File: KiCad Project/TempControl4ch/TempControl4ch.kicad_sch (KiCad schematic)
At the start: 44 parts, among them J1 Conn_01x08_Socket, U1 MAX31856, U2 MAX31856, U3 MAX31856, U4 MAX31856, U5 BluePill_Part_Like_SWD_Breako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

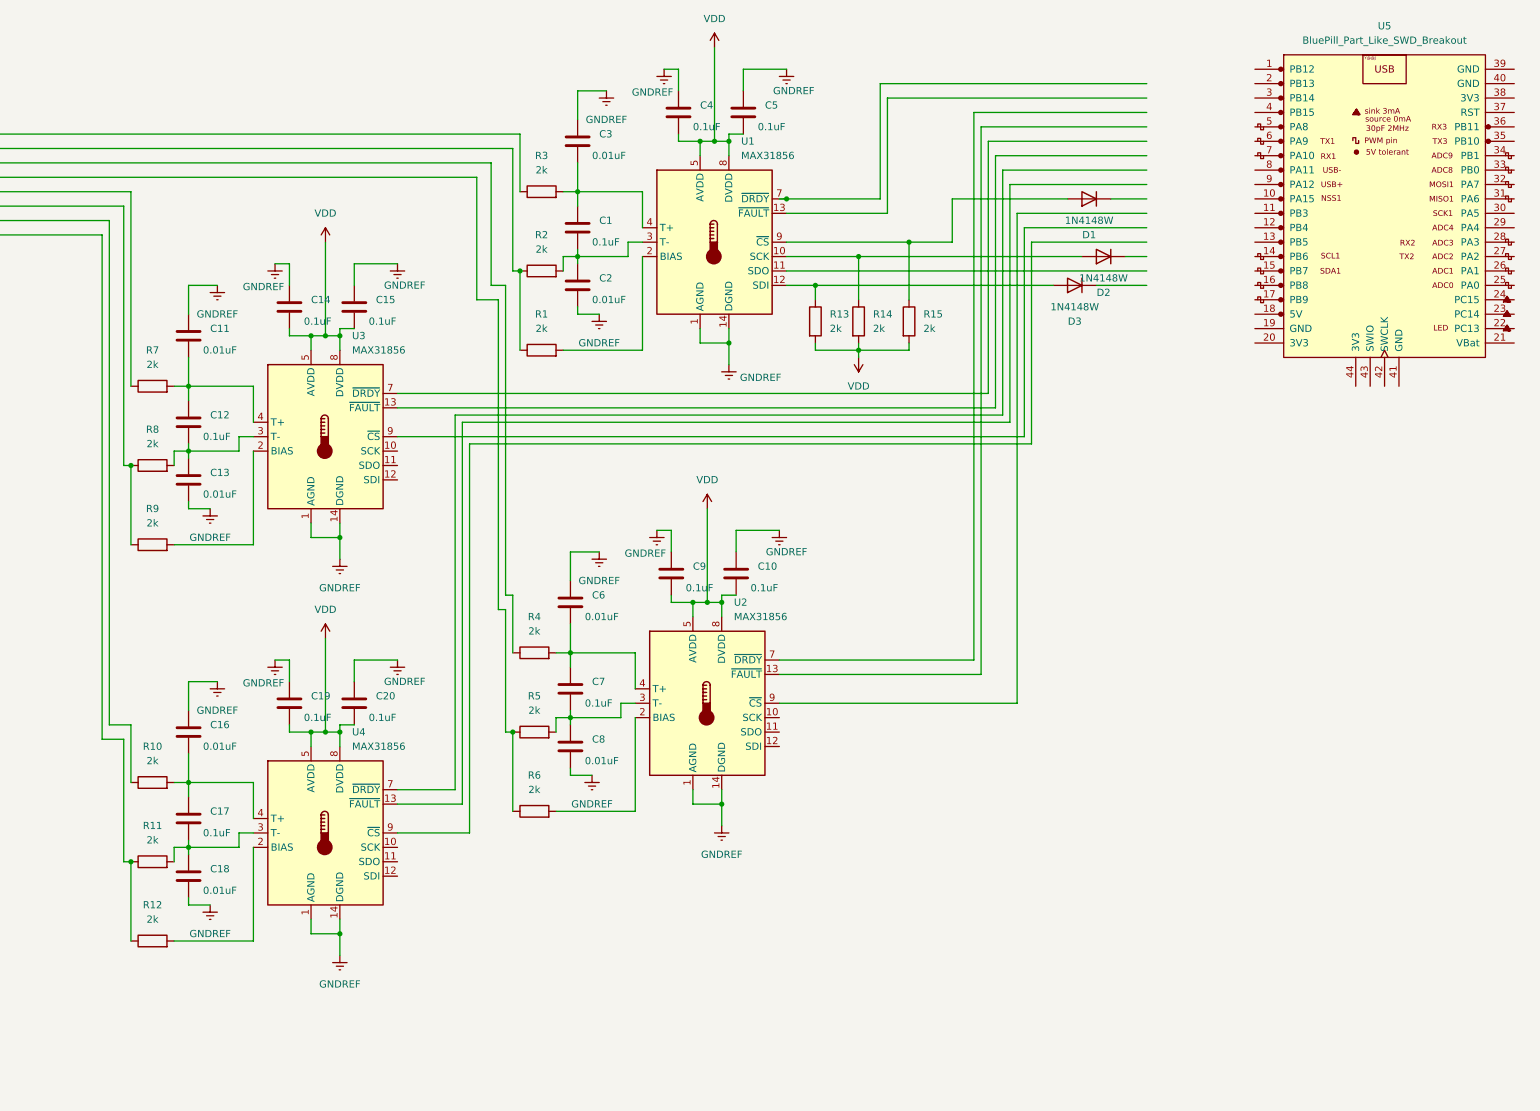
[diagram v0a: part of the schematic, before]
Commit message: added SPI connections and update schematic & pcb
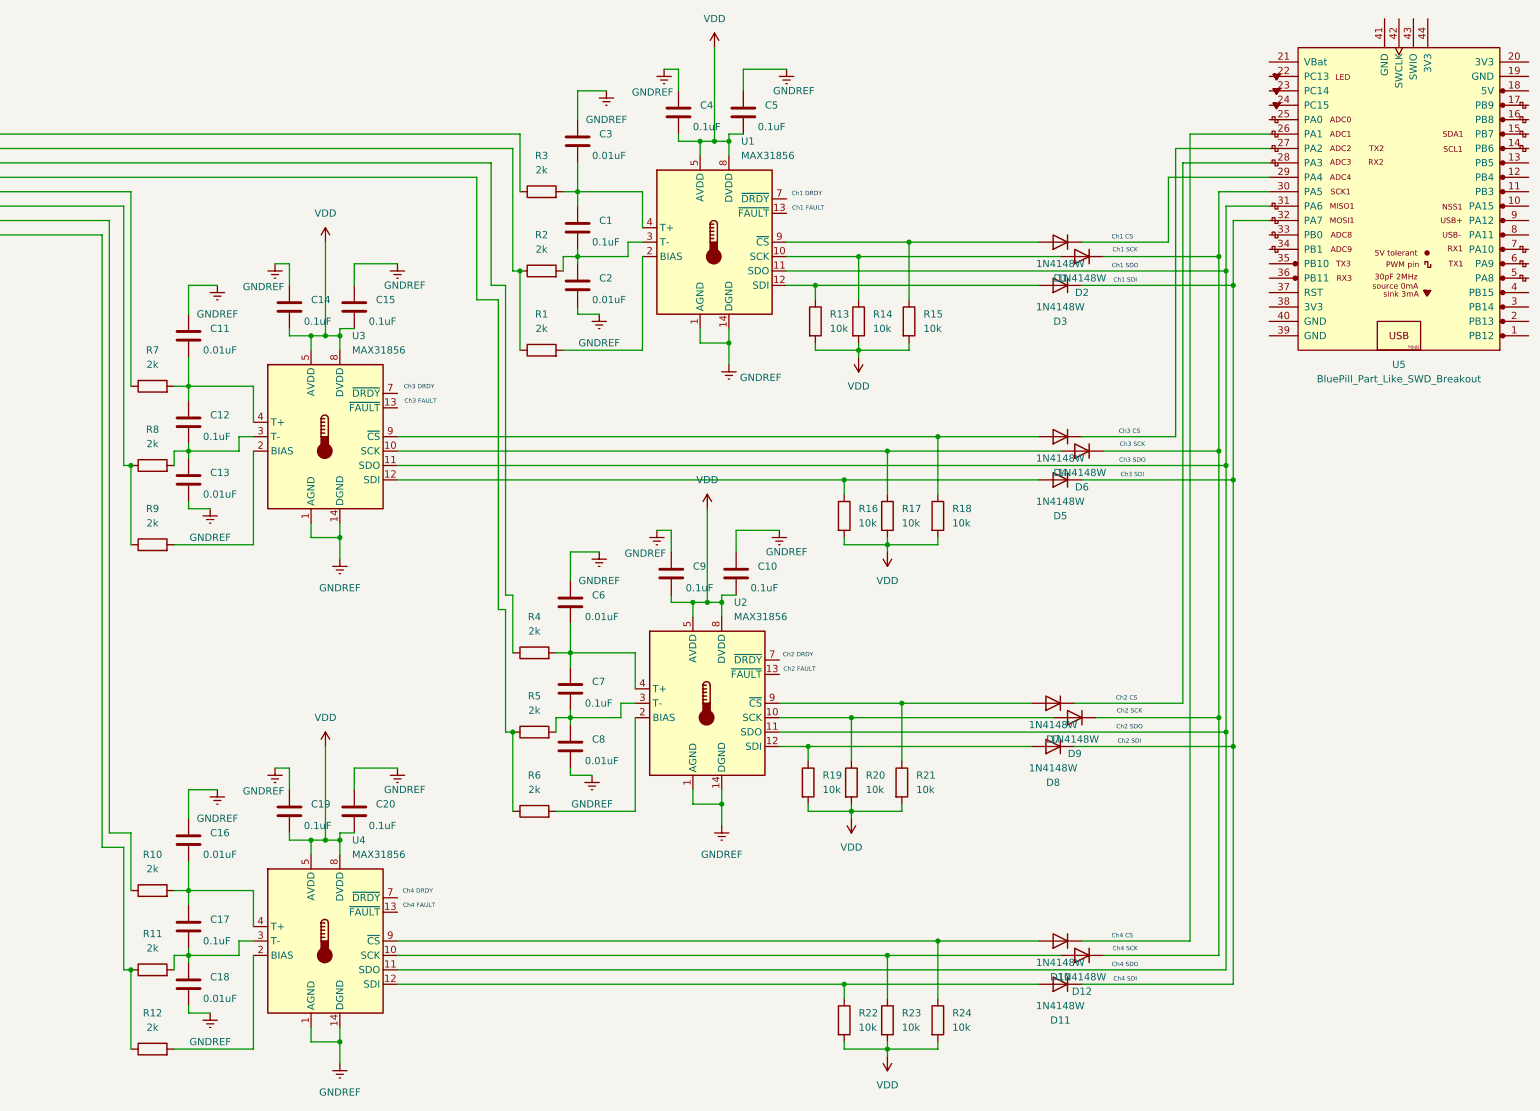
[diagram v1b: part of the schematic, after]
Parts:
- added D10, D11, D12, D4, D5, D6, D7, D8, D9: 1N4148W, Diode_SMD:D_SOD-123, symbol Diode:1N4148W
- added R16, R17, R18, R19, R20, R21, R22, R23, R24: 10k, Resistor_SMD:R_1206_3216Metric_Pad1.30x1.75mm_HandSolder, symbol Device:R
- R13, R14, R15: value 2k -> 10k
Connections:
- net VDD: now also R16.2, R17.2, R18.2, R19.2, R20.2, R21.2, R22.2, R23.2, R24.2
- net at U1.11 (SDO): now also U2.11 (SDO), U3.11 (SDO), U4.11 (SDO), U5.31 (PA6)
- net at U4.10 (SCK): now also D12.2 (A), R23.1
- net at U4.12 (SDI): now also D11.2 (A), R22.1
- net at U4.9 (~{CS}): now also D10.2 (A), R24.1
- net at D2.1 (K): now also U5.30 (PA5), D12.1 (K), D6.1 (K), D9.1 (K)
- net at U3.10 (SCK): now also D6.2 (A), R17.1
- net at U3.12 (SDI): now also D5.2 (A), R16.1
- net at U3.9 (~{CS}): now also D4.2 (A), R18.1
- net at U2.10 (SCK): now also D9.2 (A), R20.1
- net at U2.12 (SDI): now also D8.2 (A), R19.1
- net at U2.9 (~{CS}): now also D7.2 (A), R21.1
- net at D3.1 (K): now also U5.32 (PA7), D11.1 (K), D5.1 (K), D8.1 (K)
- net at D1.1 (K): now also U5.29 (PA4)
- net at U5.26 (PA1): now also D10.1 (K)
- net at U5.27 (PA2): now also D4.1 (K)
- net at U5.28 (PA3): now also D7.1 (K)
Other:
- note added: "Ch1 CS"
- note added: "Ch1 DRDY"
- note added: "Ch1 FAULT"
- note added: "Ch1 SCK"
- note added: "Ch1 SDI"
- note added: "Ch1 SDO"
- note added: "Ch2 CS"
- note added: "Ch2 DRDY"
- note added: "Ch2 FAULT"
- note added: "Ch2 SCK"
- note added: "Ch2 SDI"
- note added: "Ch2 SDO"
- note added: "Ch3 CS"
- note added: "Ch3 DRDY"
- note added: "Ch3 FAULT"
- note added: "Ch3 SCK"
- note added: "Ch3 SDI"
- note added: "Ch3 SDO"
- note added: "Ch4 CS"
- note added: "Ch4 DRDY"
- note added: "Ch4 FAULT"
- note added: "Ch4 SCK"
- note added: "Ch4 SDI"
- note added: "Ch4 SDO"
- moved on the sheet: C16, C17, C18, C19, C20, D1, D2, D3, R10, R11, R12, U4

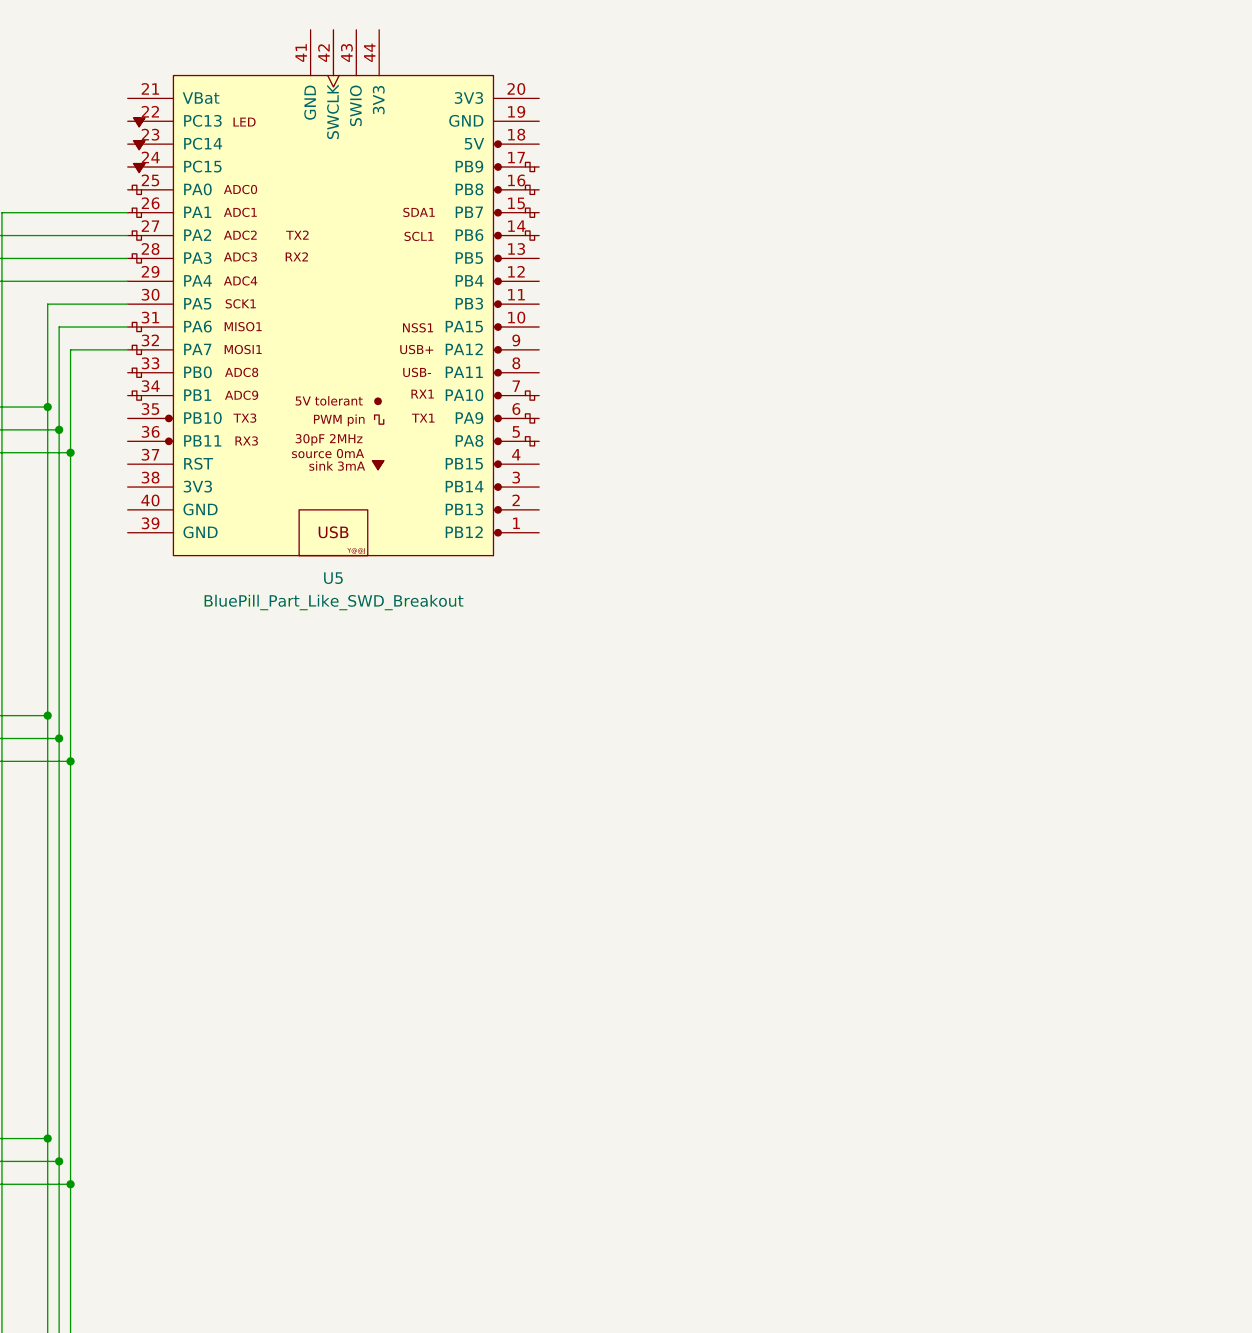
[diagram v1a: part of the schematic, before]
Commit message: added 24v to 5v converter schematic
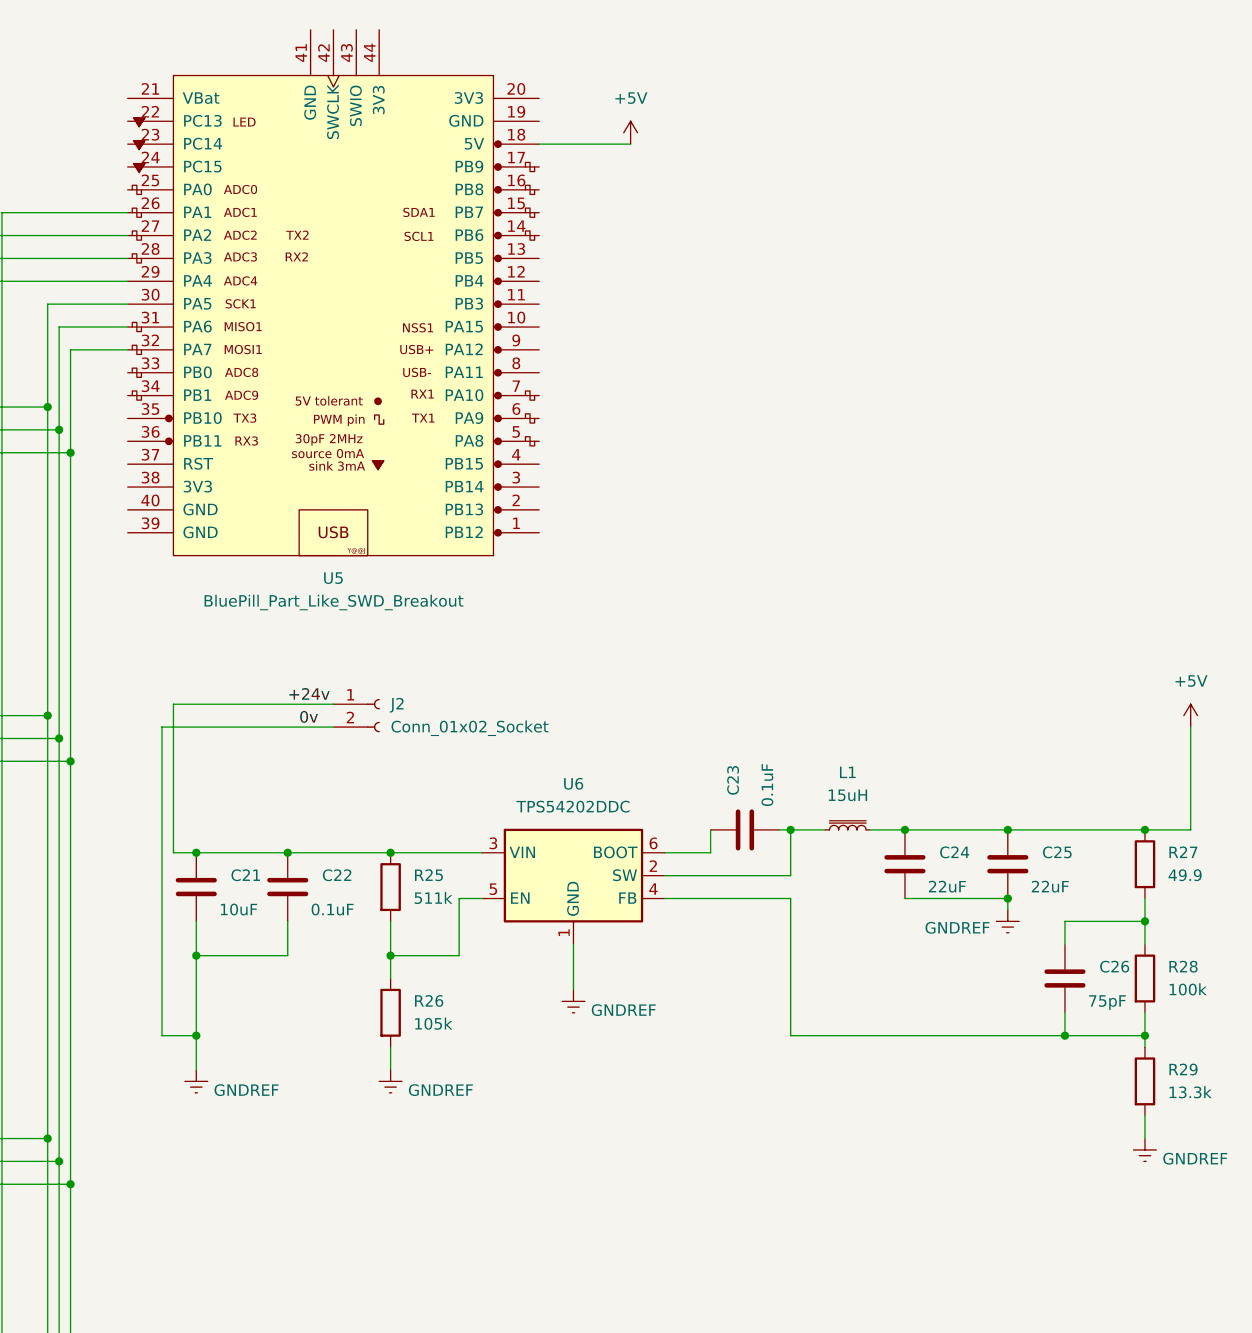
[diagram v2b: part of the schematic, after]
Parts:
- added C21: 10uF, Capacitor_SMD:C_1206_3216Metric_Pad1.33x1.80mm_HandSolder, symbol Device:C
- added C22, C23: 0.1uF, Capacitor_SMD:C_1206_3216Metric_Pad1.33x1.80mm_HandSolder, symbol Device:C
- added C24, C25: 22uF, Capacitor_SMD:C_1206_3216Metric_Pad1.33x1.80mm_HandSolder, symbol Device:C
- added C26: 75pF, Capacitor_SMD:C_1206_3216Metric_Pad1.33x1.80mm_HandSolder, symbol Device:C
- added J2: Conn_01x02_Socket, Connector_Phoenix_MC:PhoenixContact_MCV_1,5_2-G-3.5_1x02_P3.50mm_Vertical, symbol Connector:Conn_01x02_Socket
- added L1: 15uH, Inductor_SMD:L_Sumida_CDMC6D28_7.25x6.5mm, symbol Device:L_Iron_Small
- added R25: 511k, Resistor_SMD:R_1206_3216Metric_Pad1.30x1.75mm_HandSolder, symbol Device:R
- added R26: 105k, Resistor_SMD:R_1206_3216Metric_Pad1.30x1.75mm_HandSolder, symbol Device:R
- added R27: 49.9, Resistor_SMD:R_1206_3216Metric_Pad1.30x1.75mm_HandSolder, symbol Device:R
- added R28: 100k, Resistor_SMD:R_1206_3216Metric_Pad1.30x1.75mm_HandSolder, symbol Device:R
- added R29: 13.3k, Resistor_SMD:R_1206_3216Metric_Pad1.30x1.75mm_HandSolder, symbol Device:R
- added U6: TPS54202DDC, Package_TO_SOT_SMD:SOT-23-6, symbol Regulator_Switching:TPS54202DDC
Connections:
- net GNDREF: now also C21.2, C22.2, C24.2, C25.2, J2.2 (Pin_2), R26.2, R29.2, U6.1 (GND)
- net +5V: now reaches U5.18 (5V)
- net +5V: now also C24.1, C25.1, L1.2, R27.1
- new net: C26.1, R27.2, R28.1
- new net: C26.2, R28.2, R29.1, U6.4 (FB)
- new net: R25.2, R26.1, U6.5 (EN)
- new net: C23.2, L1.1, U6.2 (SW)
- new net: C23.1, U6.6 (BOOT)
- new net +24v: C21.1, C22.1, J2.1 (Pin_1), R25.1, U6.3 (VIN)
